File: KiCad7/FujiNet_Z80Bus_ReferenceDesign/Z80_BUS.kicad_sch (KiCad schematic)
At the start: 11 parts, among them IC6 7432N, IC7 7432N, J7 HOST SYSTEM HEADER, J8 DIAG-HOST_SYSTEM_BUS

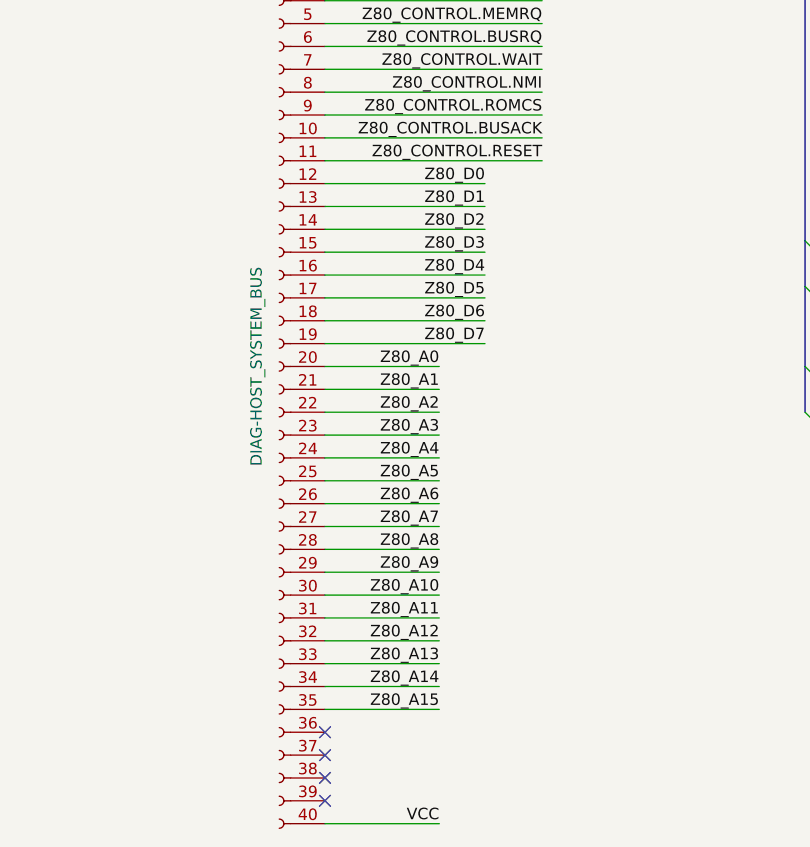
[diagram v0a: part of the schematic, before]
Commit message: KiCAD attempt to route a single board (failed)
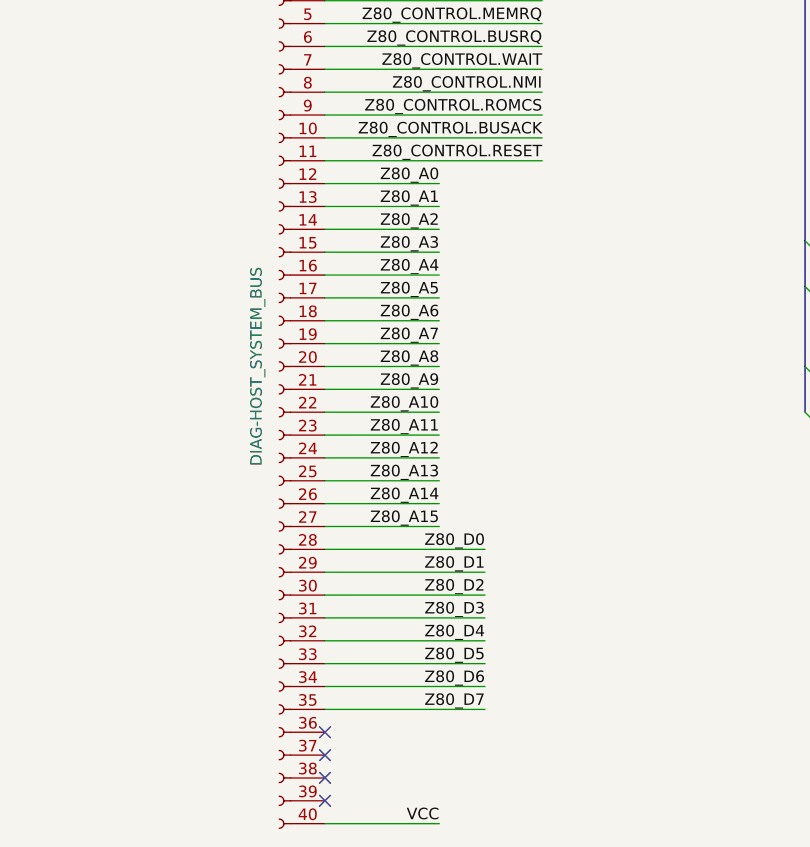
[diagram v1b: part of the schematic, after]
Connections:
- net Z80_A0: now also J8.12 (Pin_12); no longer J8.20 (Pin_20)
- net Z80_A1: now also J8.13 (Pin_13); no longer J8.21 (Pin_21)
- net Z80_A10: now also J8.22 (Pin_22); no longer J8.30 (Pin_30)
- net Z80_A11: now also J8.23 (Pin_23); no longer J8.31 (Pin_31)
- net Z80_A12: now also J8.24 (Pin_24); no longer J8.32 (Pin_32)
- net Z80_A13: now also J8.25 (Pin_25); no longer J8.33 (Pin_33)
- net Z80_A14: now also J8.26 (Pin_26); no longer J8.34 (Pin_34)
- net Z80_A15: now also J8.27 (Pin_27); no longer J8.35 (Pin_35)
- net Z80_A2: now also J8.14 (Pin_14); no longer J8.22 (Pin_22)
- net Z80_A3: now also J8.15 (Pin_15); no longer J8.23 (Pin_23)
- net Z80_A4: now also J8.16 (Pin_16); no longer J8.24 (Pin_24)
- net Z80_A5: now also J8.17 (Pin_17); no longer J8.25 (Pin_25)
- net Z80_A6: now also J8.18 (Pin_18); no longer J8.26 (Pin_26)
- net Z80_A7: now also J8.19 (Pin_19); no longer J8.27 (Pin_27)
- net Z80_A8: now also J8.20 (Pin_20); no longer J8.28 (Pin_28)
- net Z80_A9: now also J8.21 (Pin_21); no longer J8.29 (Pin_29)
- net Z80_D0: now also J8.28 (Pin_28); no longer J8.12 (Pin_12)
- net Z80_D1: now also J8.29 (Pin_29); no longer J8.13 (Pin_13)
- net Z80_D2: now also J8.30 (Pin_30); no longer J8.14 (Pin_14)
- net Z80_D3: now also J8.31 (Pin_31); no longer J8.15 (Pin_15)
- net Z80_D4: now also J8.32 (Pin_32); no longer J8.16 (Pin_16)
- net Z80_D5: now also J8.33 (Pin_33); no longer J8.17 (Pin_17)
- net Z80_D6: now also J8.34 (Pin_34); no longer J8.18 (Pin_18)
- net Z80_D7: now also J8.35 (Pin_35); no longer J8.19 (Pin_19)

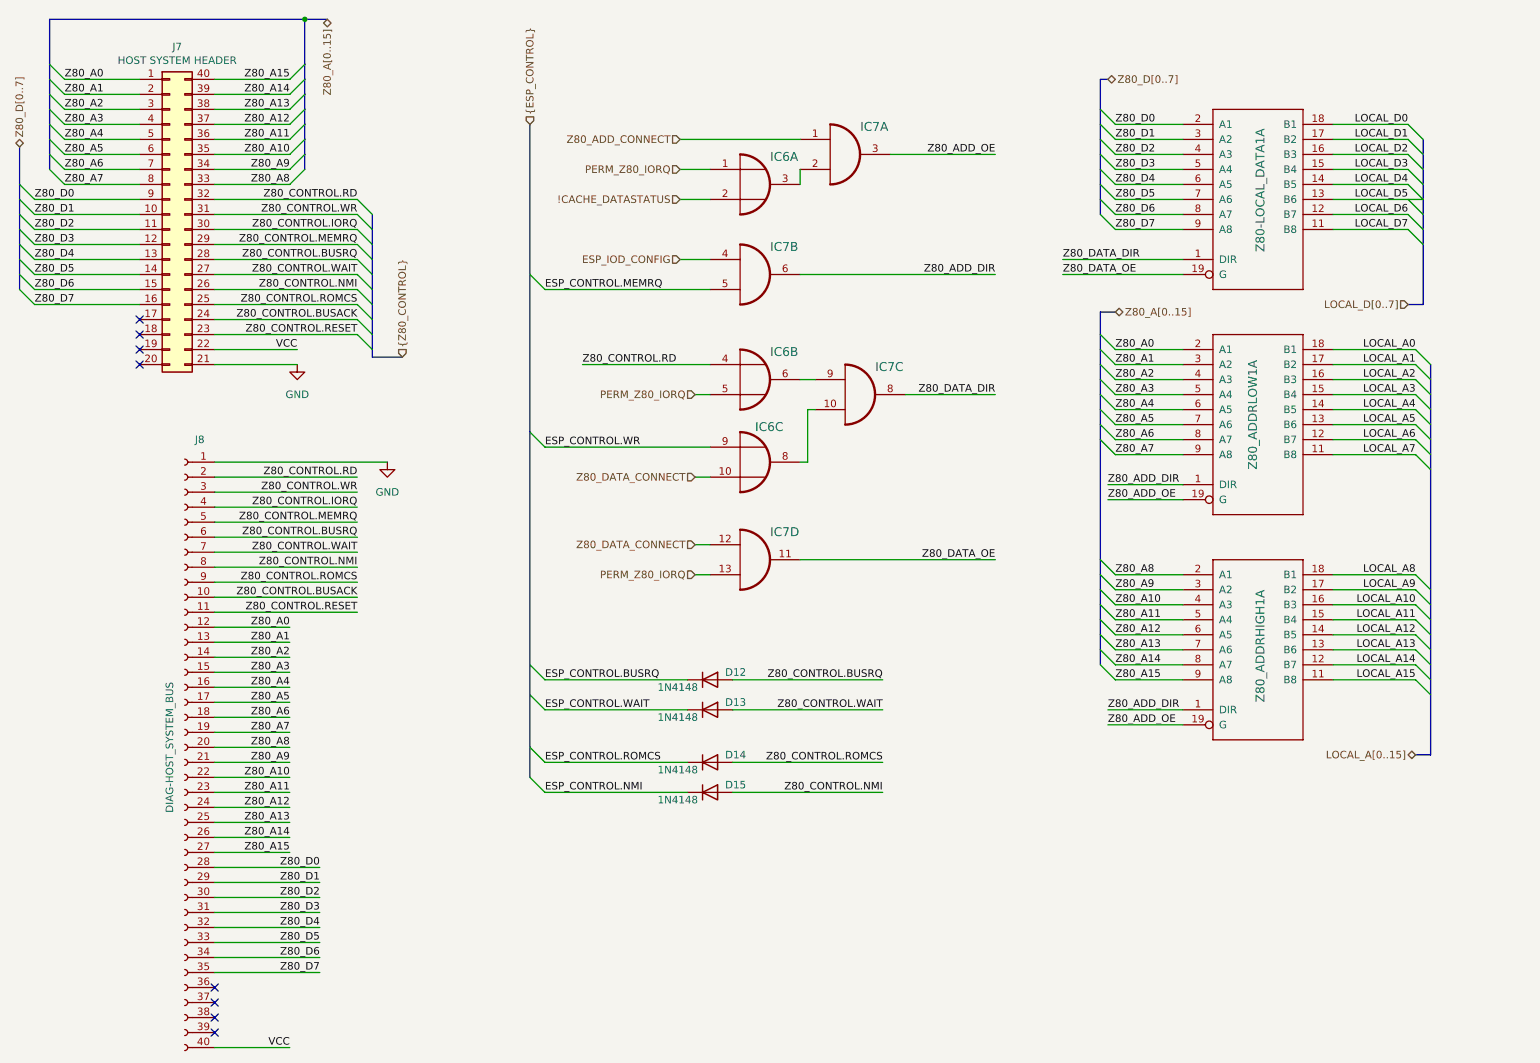
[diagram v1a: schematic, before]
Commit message: KiCad massive refactoring to enable modular PCB design
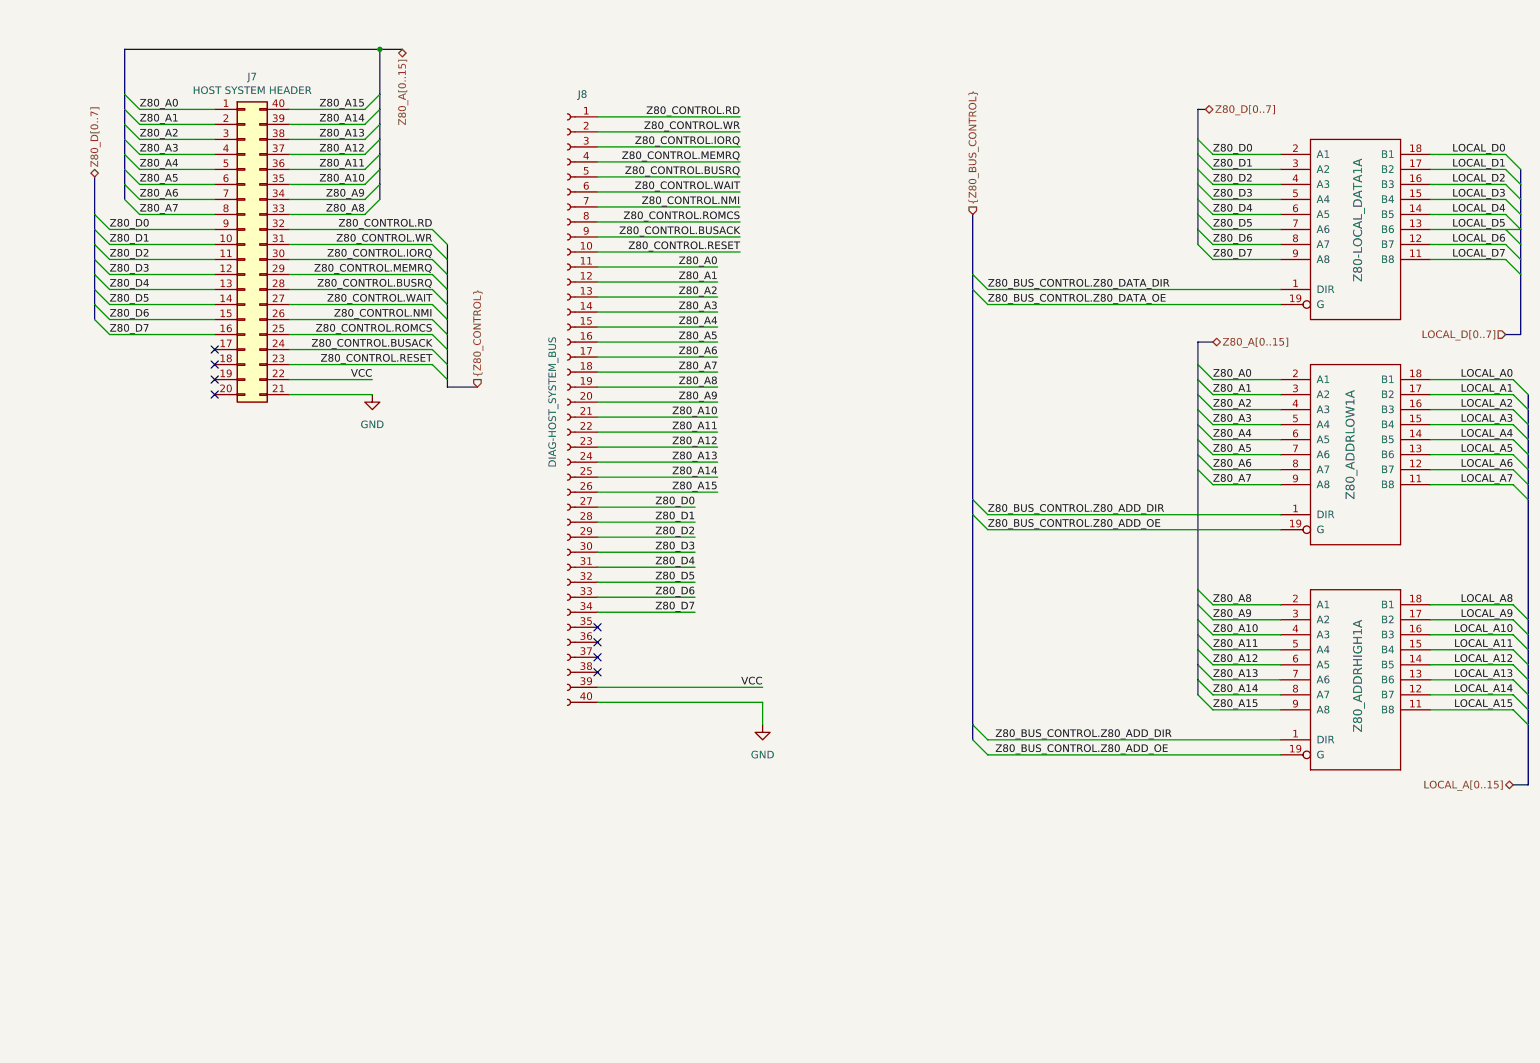
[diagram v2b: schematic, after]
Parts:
- removed D12, D13, D14, D15: 1N4148, Diode_THT:D_T-1_P5.08mm_Horizontal, symbol Device:D
- removed IC6: 7432N, Package_DIP:DIP-14_W7.62mm_Socket, symbol FujiNet_Z80Bus_Reference-rescue:7432N-Z80Decoder-eagle-import
- removed IC7: 7432N, Package_DIP:DIP-14_W7.62mm_Socket, symbol FujiNet_Z80Bus_Reference-rescue:7408N-Z80Decoder-eagle-import
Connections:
- net GND: now also J8.40 (Pin_40); no longer J8.1 (Pin_1)
- net VCC: now also J8.39 (Pin_39); no longer J8.40 (Pin_40)
- net Z80_A0: now also J8.11 (Pin_11); no longer J8.12 (Pin_12)
- net Z80_A1: now also J8.12 (Pin_12); no longer J8.13 (Pin_13)
- net Z80_A10: now also J8.21 (Pin_21); no longer J8.22 (Pin_22)
- net Z80_A11: now also J8.22 (Pin_22); no longer J8.23 (Pin_23)
- net Z80_A12: now also J8.23 (Pin_23); no longer J8.24 (Pin_24)
- net Z80_A13: now also J8.24 (Pin_24); no longer J8.25 (Pin_25)
- net Z80_A14: now also J8.25 (Pin_25); no longer J8.26 (Pin_26)
- net Z80_A15: now also J8.26 (Pin_26); no longer J8.27 (Pin_27)
- net Z80_A2: now also J8.13 (Pin_13); no longer J8.14 (Pin_14)
- net Z80_A3: now also J8.14 (Pin_14); no longer J8.15 (Pin_15)
- net Z80_A4: now also J8.15 (Pin_15); no longer J8.16 (Pin_16)
- net Z80_A5: now also J8.16 (Pin_16); no longer J8.17 (Pin_17)
- net Z80_A6: now also J8.17 (Pin_17); no longer J8.18 (Pin_18)
- net Z80_A7: now also J8.18 (Pin_18); no longer J8.19 (Pin_19)
- net Z80_A8: now also J8.19 (Pin_19); no longer J8.20 (Pin_20)
- net Z80_A9: now also J8.20 (Pin_20); no longer J8.21 (Pin_21)
- net Z80_CONTROL.BUSACK: now also J8.9 (Pin_9); no longer J8.10 (Pin_10)
- net Z80_CONTROL.BUSRQ: now also J8.5 (Pin_5); no longer J8.6 (Pin_6)
- net Z80_CONTROL.IORQ: now also J8.3 (Pin_3); no longer J8.4 (Pin_4)
- net Z80_CONTROL.MEMRQ: now also J8.4 (Pin_4); no longer J8.5 (Pin_5)
- net Z80_CONTROL.NMI: now also J8.7 (Pin_7); no longer J8.8 (Pin_8)
- net Z80_CONTROL.RD: now also J8.1 (Pin_1); no longer J8.2 (Pin_2)
- net Z80_CONTROL.RESET: now also J8.10 (Pin_10); no longer J8.11 (Pin_11)
- net Z80_CONTROL.ROMCS: now also J8.8 (Pin_8); no longer J8.9 (Pin_9)
- net Z80_CONTROL.WAIT: now also J8.6 (Pin_6); no longer J8.7 (Pin_7)
- net Z80_CONTROL.WR: now also J8.2 (Pin_2); no longer J8.3 (Pin_3)
- net Z80_D0: now also J8.27 (Pin_27); no longer J8.28 (Pin_28)
- net Z80_D1: now also J8.28 (Pin_28); no longer J8.29 (Pin_29)
- net Z80_D2: now also J8.29 (Pin_29); no longer J8.30 (Pin_30)
- net Z80_D3: now also J8.30 (Pin_30); no longer J8.31 (Pin_31)
- net Z80_D4: now also J8.31 (Pin_31); no longer J8.32 (Pin_32)
- net Z80_D5: now also J8.32 (Pin_32); no longer J8.33 (Pin_33)
- net Z80_D6: now also J8.33 (Pin_33); no longer J8.34 (Pin_34)
- net Z80_D7: now also J8.34 (Pin_34); no longer J8.35 (Pin_35)
- net Z80_ADD_DIR renamed Z80_BUS_CONTROL.Z80_ADD_DIR
- net Z80_ADD_OE renamed Z80_BUS_CONTROL.Z80_ADD_OE
- net Z80_DATA_DIR renamed Z80_BUS_CONTROL.Z80_DATA_DIR
- net Z80_DATA_OE renamed Z80_BUS_CONTROL.Z80_DATA_OE
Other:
- moved on the sheet: J7, J8, Z80-LOCAL_DATA1A, Z80_ADDRHIGH1A, Z80_ADDRLOW1A

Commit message: Kicad Symbols error fixes and ERC bug fixes
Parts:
- J8: symbol FujiNet_Z80Bus_Reference-rescue:Conn_01x40_Female-Connector -> Connector:Conn_01x40_Socket
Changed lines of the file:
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@@
     (effects (font (size 1.27 1.27)) (justify right))
   )
-  (symbol (lib_id "FujiNet_Z80Bus_Reference-rescue:Conn_01x40_Female-Connector") (at 111.76 82.55 0) (mirror y) (unit 1)
+  (symbol (lib_id "Connector:Conn_01x40_Socket") (at 111.76 82.55 0) (mirror y) (unit 1)
     (in_bom yes) (on_board yes) (dnp no)
     (property "Reference" "J8" (at 114.3 30.48 0)

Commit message: KiCad - ALMOST ERROR FREE!!!!
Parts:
- Z80-LOCAL_DATA1, Z80_ADDRHIGH1, Z80_ADDRLOW1: symbol FujiNet_Z80Bus_Reference-rescue:74245N-Z80Decoder-eagle-import -> 74xx:74HC245
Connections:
- net GND: now also Z80-LOCAL_DATA1.10 (GND), Z80_ADDRHIGH1.10 (GND), Z80_ADDRLOW1.10 (GND)
- net HOST VCC: now reaches J7.20 (Pin_20)
- net HOST VCC: now also J8.39 (Pin_39)
- net VCC: no longer names the net of J7.22 (Pin_22)
- net VCC: no longer J8.39 (Pin_39)
- new net +5V: Z80-LOCAL_DATA1.20 (VCC), Z80_ADDRHIGH1.20 (VCC), Z80_ADDRLOW1.20 (VCC)
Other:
- moved on the sheet: J7, J8

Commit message: KiCAD PCB layout testing
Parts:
- Z80-LOCAL_DATA1, Z80_ADDRHIGH1, Z80_ADDRLOW1: value 74245N -> 74HC245N
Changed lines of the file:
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@@
       (effects (font (size 1.4986 1.4986)) (justify left bottom))
     )
-    (property "Value" "74245N" (at 74.93 53.34 0)
+    (property "Value" "74HC245N" (at 74.93 53.34 0)
       (effects (font (size 1.4986 1.4986)) (justify left bottom) hide)
     )
@@
       (effects (font (size 1.4986 1.4986)) (justify left bottom))
     )
-    (property "Value" "74245N" (at 166.37 53.34 0)
+    (property "Value" "74HC245N" (at 166.37 53.34 0)
       (effects (font (size 1.4986 1.4986)) (justify left bottom) hide)
     )
@@
       (effects (font (size 1.4986 1.4986)) (justify left bottom))
     )
-    (property "Value" "74245N" (at 120.65 53.34 0)
+    (property "Value" "74HC245N" (at 120.65 53.34 0)
       (effects (font (size 1.4986 1.4986)) (justify left bottom) hide)
     )
